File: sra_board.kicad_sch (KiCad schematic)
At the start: 168 parts, among them J1 Conn_01x14_Pin, J10 Conn_01x03_Pin, J11 Conn_01x08_Pin, J12 Conn_01x07_Pin, J13 Conn_01x04_Pin, J14 Conn_01x02_Pin, J15 Conn_01x02_Pin, J16 Conn_01x02_Pin, J17 USB_C_Receptacle_USB2.0_16P, J2 Conn_01x14_Pin, J3 Conn_01x03_Pin, J4 Conn_01x04_Pin, J5 Conn_01x03_Pin, J6 Conn_01x03_Pin, J7 Conn_01x03_Pin, J8 Conn_01x03_Pin, J9 Conn_01x03_Pin, Q1 SS8050, Q2 SS8050, Q3 AO4435, Q4 AO4468, SW3 SW_IO0, SW4 Switch, SW5 SW_EN, SW6 Switch, U1 MAX7219CWG_T, U2 ESP32-WROOM-32E, U3 TB6612FNG H-bridge Motor Driv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, U4 ME6211C33M5, U5 CH340C, U6 TPS562202, U7 CN3303

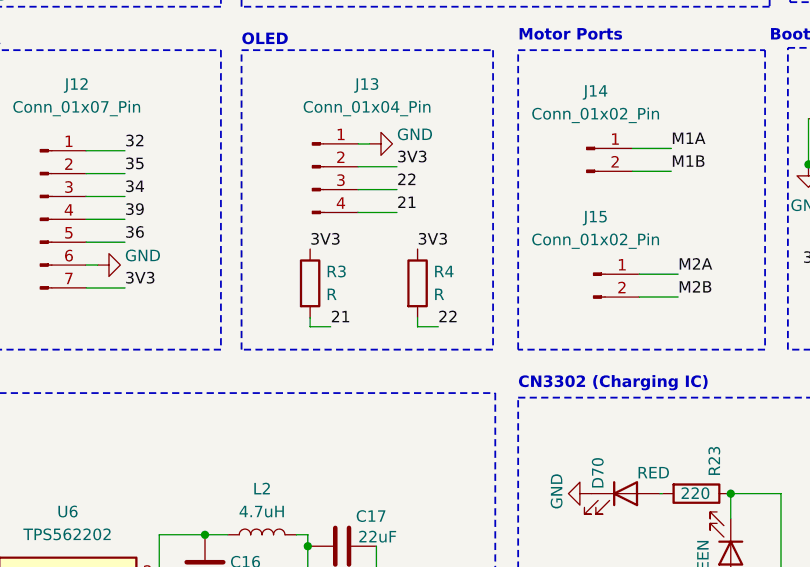
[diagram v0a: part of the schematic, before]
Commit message: Added pullup resistor values to OLED
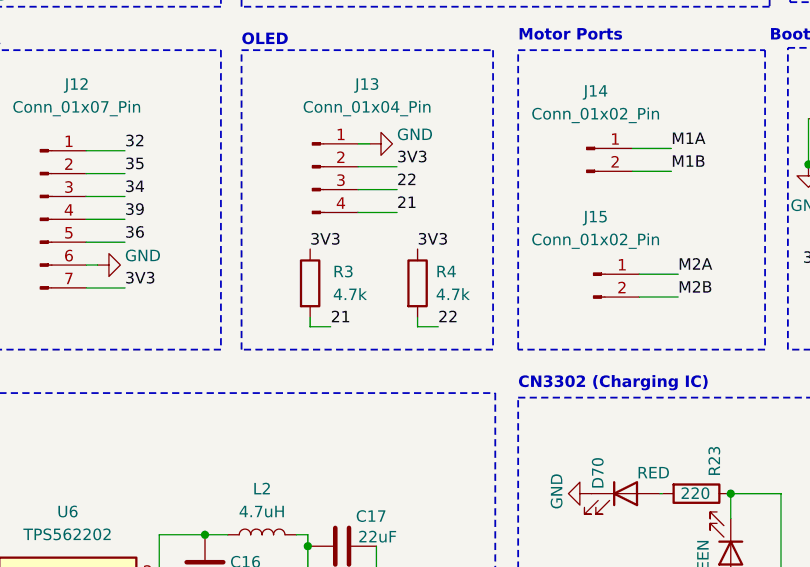
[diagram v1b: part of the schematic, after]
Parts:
- R3, R4: value R -> 4.7k
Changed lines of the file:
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@@
 		(fields_autoplaced yes)
 		(property "Reference" "R3"
-			(at 83.058 131.3179 0)
-			(show_name no)
-			(do_not_autoplace no)
-			(effects
-				(font
-					(size 1.27 1.27)
-				)
-				(justify left)
-			)
-		)
-		(property "Value" "R"
-			(at 83.058 133.8579 0)
+			(at 83.82 131.3179 0)
+			(show_name no)
+			(do_not_autoplace no)
+			(effects
+				(font
+					(size 1.27 1.27)
+				)
+				(justify left)
+			)
+		)
+		(property "Value" "4.7k"
+			(at 83.82 133.8579 0)
 			(show_name no)
 			(do_not_autoplace no)
@@
 		(fields_autoplaced yes)
 		(property "Reference" "R4"
-			(at 94.996 131.3179 0)
-			(show_name no)
-			(do_not_autoplace no)
-			(effects
-				(font
-					(size 1.27 1.27)
-				)
-				(justify left)
-			)
-		)
-		(property "Value" "R"
-			(at 94.996 133.8579 0)
-			(show_name no)
-			(do_not_autoplace no)
+			(at 95.25 131.3179 0)
+			(show_name no)
+			(do_not_autoplace no)
+			(effects
+				(font
+					(size 1.27 1.27)
+				)
+				(justify left)
+			)
+		)
+		(property "Value" "4.7k"
+			(at 95.25 133.8579 0)
+			(show_name no)
+			(do_not_autoplace no)

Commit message: Added footprints
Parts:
- C1, C10, C11, C2, C21, C22, C23, C24, C3, C4, C5, C6, C7: footprint (none) -> Capacitor_SMD:C_0603_1608Metric
- C12, C13, C14, C15, C16, C17, C18, C8, C9: footprint Capacitor_SMD:C_0805_2012Metric -> Capacitor_SMD:C_0603_1608Metric
- D1, D10, D11, D12, D13, D14, D15, D16, D17, D18, D19, D2, D20, D21, D22, D23, D24, D25, D26, D27, D28, D29, D3, D30, D31, D32, D33, D34, D35, D36, D37, D38, D39, D4, D40, D41, D42, D43, D44, D45, D46, D47, D48, D49, D5, D50, D51, D52, D53, D54, D55, D56, D57, D58, D59, D6, D60, D61, D62, D63, D64, D65, D67, D7, D70, D8, D9: footprint (none) -> LED_SMD:LED_0603_1608Metric
- H1, H2, H3, H4, H5, H6: footprint (none) -> MountingHole:MountingHole_3.2mm_M3
- J1, J2: footprint (none) -> Connector_PinHeader_2.54mm:PinHeader_1x14_P2.54mm_Vertical_SMD_Pin1Left
- R1, R11, R12, R13, R14, R15, R2, R23, R3, R4, R6, R7, R8, R9: footprint (none) -> Resistor_SMD:R_0603_1608Metric
- R10, R5: footprint Resistor_SMD:R_0805_2012Metric_Pad1.20x1.40mm_HandSolder -> Resistor_SMD:R_0603_1608Metric
- R17, R18, R19: footprint Resistor_SMD:R_0805_2012Metric -> Resistor_SMD:R_0603_1608Metric
- TP1, TP2, TP3, TP4, TP5: footprint (none) -> TestPoint:TestPoint_Pad_D1.0mm

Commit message: Added footprints
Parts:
- J1, J2: footprint Connector_PinHeader_2.54mm:PinHeader_1x14_P2.54mm_Vertical_SMD_Pin1Left -> Connector_PinHeader_2.54mm:PinHeader_1x14_P2.54mm_Vertical
- J10, J3, J5, J6, J7, J8, J9: footprint (none) -> Connector_PinHeader_2.54mm:PinHeader_1x03_P2.54mm_Vertical
- J11: footprint (none) -> Connector_PinSocket_2.54mm:PinSocket_1x08_P2.54mm_Vertical
- J12: footprint (none) -> Connector_JST:JST_EH_S7B-EH_1x07_P2.50mm_Horizontal
- J13, J4: footprint (none) -> Connector_PinHeader_2.54mm:PinHeader_1x04_P2.54mm_Vertical
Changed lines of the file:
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@@
 			)
 		)
-		(property "Footprint" "Connector_PinHeader_2.54mm:PinHeader_1x14_P2.54mm_Vertical_SMD_Pin1Left"
+		(property "Footprint" "Connector_PinHeader_2.54mm:PinHeader_1x14_P2.54mm_Vertical"
 			(at 112.014 46.99 0)
 			(hide yes)
@@
 			)
 		)
-		(property "Footprint" ""
+		(property "Footprint" "Connector_JST:JST_EH_S7B-EH_1x07_P2.50mm_Horizontal"
 			(at 51.308 125.476 0)
 			(hide yes)
@@
 			)
 		)
-		(property "Footprint" ""
+		(property "Footprint" "Connector_PinHeader_2.54mm:PinHeader_1x04_P2.54mm_Vertical"
 			(at 88.138 83.82 0)
 			(hide yes)
@@
 			)
 		)
-		(property "Footprint" ""
+		(property "Footprint" "Connector_PinHeader_2.54mm:PinHeader_1x03_P2.54mm_Vertical"
 			(at 222.504 62.23 0)
 			(hide yes)
@@
 			)
 		)
-		(property "Footprint" ""
+		(property "Footprint" "Connector_PinHeader_2.54mm:PinHeader_1x03_P2.54mm_Vertical"
 			(at 238.506 62.738 0)
 			(hide yes)
@@
 			)
 		)
-		(property "Footprint" ""
+		(property "Footprint" "Connector_PinHeader_2.54mm:PinHeader_1x03_P2.54mm_Vertical"
 			(at 188.214 90.932 0)
 			(hide yes)
@@
 			)
 		)
-		(property "Footprint" ""
+		(property "Footprint" "Connector_PinSocket_2.54mm:PinSocket_1x08_P2.54mm_Vertical"
 			(at 22.352 125.73 0)
 			(hide yes)
@@
 			)
 		)
-		(property "Footprint" ""
+		(property "Footprint" "Connector_PinHeader_2.54mm:PinHeader_1x03_P2.54mm_Vertical"
 			(at 142.748 90.932 0)
 			(hide yes)
@@
 			)
 		)
-		(property "Footprint" ""
+		(property "Footprint" "Connector_PinHeader_2.54mm:PinHeader_1x04_P2.54mm_Vertical"
 			(at 81.534 119.634 0)
 			(hide yes)
@@
 			)
 		)
-		(property "Footprint" "Connector_PinHeader_2.54mm:PinHeader_1x14_P2.54mm_Vertical_SMD_Pin1Left"
+		(property "Footprint" "Connector_PinHeader_2.54mm:PinHeader_1x14_P2.54mm_Vertical"
 			(at 89.154 46.736 0)
 			(hide yes)
@@
 			)
 		)
-		(property "Footprint" ""
+		(property "Footprint" "Connector_PinHeader_2.54mm:PinHeader_1x03_P2.54mm_Vertical"
 			(at 174.498 90.678 0)
 			(hide yes)
@@
 			)
 		)
-		(property "Footprint" ""
+		(property "Footprint" "Connector_PinHeader_2.54mm:PinHeader_1x03_P2.54mm_Vertical"
 			(at 204.724 62.738 0)
 			(hide yes)
@@
 			)
 		)
-		(property "Footprint" ""
+		(property "Footprint" "Connector_PinHeader_2.54mm:PinHeader_1x03_P2.54mm_Vertical"
 			(at 159.258 90.932 0)
 			(hide yes)
